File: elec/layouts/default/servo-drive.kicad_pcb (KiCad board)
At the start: 4 copper layers, 37.5 x 39.9 mm, 125 parts, among them U2 8Mhz

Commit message: Placement 90% complete
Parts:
- removed R2, R5: 10kOhm, Resistor_SMD:R_0402_1005Metric
- removed U19: , lib:SC-70-6_L2.1-W1.3-P0.65-LS2.1-BR
- added C23: 10uF, Capacitor_SMD:C_0603_1608Metric, F.Cu at (177.0, 101.6)
- C11, C20, C21, C22, C40, C5, R13, R14, R44, R45, R46, R50, R51, U21, U25, U26: moved to B.Cu
- C16: moved to F.Cu
- C26: footprint Capacitor_SMD:C_0805_2012Metric -> Capacitor_SMD:C_0603_1608Metric; moved to F.Cu
- C29: footprint Capacitor_SMD:C_0805_2012Metric -> Capacitor_SMD:C_0603_1608Metric
- C31, C32: value 22uF -> 10uF; footprint Capacitor_SMD:C_0805_2012Metric -> Capacitor_SMD:C_0603_1608Metric; moved to F.Cu
- C8: value (none) -> 10uF; footprint Capacitor_SMD:C_0402_1005Metric -> Capacitor_SMD:C_0603_1608Metric
- R12, R49: value (none) -> 45kOhm
- R25: value (none) -> 1kOhm; moved to B.Cu
- R26: value (none) -> 45kOhm; moved to B.Cu
- R48, R6: value (none) -> 1kOhm
- U17: footprint lib:CONN-SMD_4P-P1.00_SM04B-SRSS-TB-LF-SN -> lib:LED-SMD_4P-L4.0-W1.4_SK6805SIDE-S; moved to B.Cu
- U4: footprint lib:SOIC-8_L5.0-W4.0-P1.27-LS6.0-BL -> Package_TO_SOT_SMD:SOT-23-5
- moved C39 99.8 mm to (233.5, 85.1)
- moved R14 97.8 mm to (226.7, 86.9)
- moved C21 96.5 mm to (233.5, 85.4)
- moved R13 96.2 mm to (226.7, 87.9), turned to 180 degrees
- moved C20 96.0 mm to (233.5, 83.0)
- moved C22 90.7 mm to (233.8, 105.1)
- moved R45 82.8 mm to (226.7, 92.4)
- moved R44 82.1 mm to (226.7, 91.4), turned to 180 degrees
- moved C2 80.2 mm to (217.1, 111.3), turned to -90 degrees
- moved R1 80.1 mm to (217.1, 109.4), turned to -90 degrees
- moved R51 71.0 mm to (226.7, 105.0)
- moved R50 70.4 mm to (226.7, 104.0), turned to 180 degrees
- moved U25 68.2 mm to (213.0, 106.4)
- moved U27 56.9 mm to (210.9, 119.1)
- moved U4 56.6 mm to (219.3, 109.8), turned to 90 degrees
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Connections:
- C10 pad 1: servo_drive.ato:ServoDrive.power_stage.current_sense_a.out -> servo_drive.ato:ServoDrive.power_stage.i_fb_a
- C11 pad 1: servo_drive.ato:ServoDrive.power_stage.current_sense_b.out -> servo_drive.ato:ServoDrive.power_stage.i_fb_b
- C12 pad 1: servo_drive.ato:ServoDrive.power_stage.current_sense_c.out -> servo_drive.ato:ServoDrive.power_stage.i_fb_c
- C2 pad 1: servo_drive.ato:ServoDrive.power_stage.reference.buffer.in_p_a-filter.out -> servo_drive.ato:ServoDrive.power_stage.reference.buffer.in_p-filter.out
- C8 pad 1: servo_drive.ato:ServoDrive.power_stage.reference.buffer.in_p_b-half_ref.output -> servo_drive.ato:ServoDrive.v_10
- R1 pad 2: servo_drive.ato:ServoDrive.power_stage.reference.buffer.in_p_a-filter.out -> servo_drive.ato:ServoDrive.power_stage.reference.buffer.in_p-filter.out
- R14 pad 2: servo_drive.ato:ServoDrive.v_3 -> servo_drive.ato:ServoDrive.power_stage.v_ref
- R16 pad 2: servo_drive.ato:ServoDrive.power_stage.current_sense_a.out -> servo_drive.ato:ServoDrive.power_stage.i_fb_a
- R45 pad 2: servo_drive.ato:ServoDrive.v_3 -> servo_drive.ato:ServoDrive.power_stage.v_ref
- R46 pad 2: servo_drive.ato:ServoDrive.power_stage.current_sense_b.out -> servo_drive.ato:ServoDrive.power_stage.i_fb_b
- R51 pad 2: servo_drive.ato:ServoDrive.v_3 -> servo_drive.ato:ServoDrive.power_stage.v_ref
- R52 pad 2: servo_drive.ato:ServoDrive.power_stage.current_sense_c.out -> servo_drive.ato:ServoDrive.power_stage.i_fb_c
- U15 pad 38: servo_drive.ato:ServoDrive.micro_kit.micro.PA15 -> servo_drive.ato:ServoDrive.position_sensor.cs
- U15 pad 39: servo_drive.ato:ServoDrive.micro_kit.micro.PB3 -> servo_drive.ato:ServoDrive.position_sensor.sck
- U15 pad 40: servo_drive.ato:ServoDrive.micro_kit.micro.PB4 -> servo_drive.ato:ServoDrive.position_sensor.miso
- U15 pad 41: servo_drive.ato:ServoDrive.micro_kit.micro.PB5 -> servo_drive.ato:ServoDrive.position_sensor.mosi
- U15 pad 42: servo_drive.ato:ServoDrive.i2c_active_terminator.bus2-stemma.scl -> servo_drive.ato:ServoDrive.micro_kit.micro.PB6
- U15 pad 43: servo_drive.ato:ServoDrive.i2c_active_terminator.bus1-stemma.sda -> servo_drive.ato:ServoDrive.micro_kit.micro.PB7
- U17 pad 1: servo_drive.ato:ServoDrive.gnd -> servo_drive.ato:ServoDrive.v_5
- U17 pad 2: servo_drive.ato:ServoDrive.v_3 -> servo_drive.ato:ServoDrive.gnd
- U17 pad 3: servo_drive.ato:ServoDrive.i2c_active_terminator.bus1-stemma.sda -> servo_drive.ato:ServoDrive.led2.data_out
- U17 pad 4: servo_drive.ato:ServoDrive.i2c_active_terminator.bus2-stemma.scl -> servo_drive.ato:ServoDrive.led.data_out-led2.data_in
- U4 pad 1: servo_drive.ato:ServoDrive.power_stage.reference.buffer.in_n_a-out_a -> servo_drive.ato:ServoDrive.power_stage.reference.buffer.in_p-filter.out
- U4 pad 2: servo_drive.ato:ServoDrive.power_stage.reference.buffer.in_n_a-out_a -> servo_drive.ato:ServoDrive.gnd
- U4 pad 3: servo_drive.ato:ServoDrive.power_stage.reference.buffer.in_p_a-filter.out -> servo_drive.ato:ServoDrive.power_stage.v_ref
- U4 pad 4: servo_drive.ato:ServoDrive.gnd -> servo_drive.ato:ServoDrive.power_stage.v_ref
- U4 pad 5: servo_drive.ato:ServoDrive.power_stage.reference.buffer.in_p_b-half_ref.output -> servo_drive.ato:ServoDrive.v_3
- U5 pad 3: servo_drive.ato:ServoDrive.led.data_out -> servo_drive.ato:ServoDrive.led.data_out-led2.data_in
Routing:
- net servo_drive.ato:ServoDrive.canbus.CANL-canbus_conn_1.scl-canbus_conn_2.scl: track 0.00 -> 21.0 mm, vias 0 -> 1
- net servo_drive.ato:ServoDrive.canbus.CANH-canbus_conn_1.sda-canbus_conn_2.sda: track 0.00 -> 11.0 mm, vias 0 -> 1
- net servo_drive.ato:ServoDrive.v_3: track 1.30 -> 7.06 mm
- net servo_drive.ato:ServoDrive.buck.SGND: track 5.24 -> 10.6 mm, vias 0 -> 2
- net servo_drive.ato:ServoDrive.buck.buck_converter.VCC: track 0.00 -> 5.29 mm
- net servo_drive.ato:ServoDrive.micro_kit.osc.out: track 0.00 -> 4.74 mm
- net servo_drive.ato:ServoDrive.micro_kit.micro.PD0_OSC_IN-osc.in: track 0.00 -> 4.74 mm
- net servo_drive.ato:ServoDrive.micro_kit.micro.PD1_OSC_OUT: track 0.00 -> 4.26 mm
- net servo_drive.ato:ServoDrive.power_stage.current_sense_c.feedback_div.gnd-opamp.out-output_filter.in: track 0.00 -> 4.03 mm
- net servo_drive.ato:ServoDrive.power_stage.current_sense_c.feedback_div.output-opamp.in_n: track 0.00 -> 3.55 mm
- net servo_drive.ato:ServoDrive.gnd: track 30.9 -> 27.7 mm, vias 38 -> 37
- net servo_drive.ato:ServoDrive.power_stage.current_sense_c.bias_div.output-opamp.in_p: track 0.00 -> 2.45 mm
- net servo_drive.ato:ServoDrive.power_stage.v_ref: track 0.00 -> 2.28 mm
- net servo_drive.ato:ServoDrive.power_stage.reference.buffer.in_p-filter.out: track 0.00 -> 2.20 mm
- net servo_drive.ato:ServoDrive.buck.buck_converter.SS: track 0.00 -> 1.95 mm
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
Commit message: layout
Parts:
- removed C33: , Capacitor_SMD:C_0402_1005Metric
- removed C34: 2nF, Capacitor_SMD:C_0402_1005Metric
- removed R27: 10kOhm, Resistor_SMD:R_0402_1005Metric
- removed R28: 1kOhm, Resistor_SMD:R_0402_1005Metric
- C1, C18, C3, C8, R24: moved to B.Cu
- moved C8 64.6 mm to (240.2, 112.3), turned to -90 degrees
- moved C19 54.7 mm to (213.1, 100.8), turned to 180 degrees
- moved C1 48.6 mm to (213.1, 101.8), turned to 180 degrees
- moved C18 46.4 mm to (207.4, 94.9), turned to -90 degrees
- moved C23 42.7 mm to (219.6, 97.3), turned to -90 degrees
- moved C32 41.1 mm to (221.0, 90.7), turned to -90 degrees
- moved S1 39.1 mm to (213.8, 88.7)
- moved C3 38.2 mm to (216.9, 96.3), turned to -45 degrees
- moved R24 37.8 mm to (218.9, 84.2), turned to 45 degrees
- moved R11 33.1 mm to (207.9, 88.5), turned to -90 degrees
- moved C31 29.6 mm to (220.9, 101.6), turned to 90 degrees
- moved C5 28.7 mm to (241.6, 111.8), turned to -90 degrees
- moved C17 26.4 mm to (214.4, 114.3)
- moved C13 25.7 mm to (214.3, 113.3)
- moved R23 25.2 mm to (208.0, 92.4), turned to 90 degrees
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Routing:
- net servo_drive.ato:ServoDrive.micro_kit.micro.PD0_OSC_IN-osc.in: track 4.74 -> 6.66 mm
- net servo_drive.ato:ServoDrive.gnd: track 27.7 -> 29.3 mm

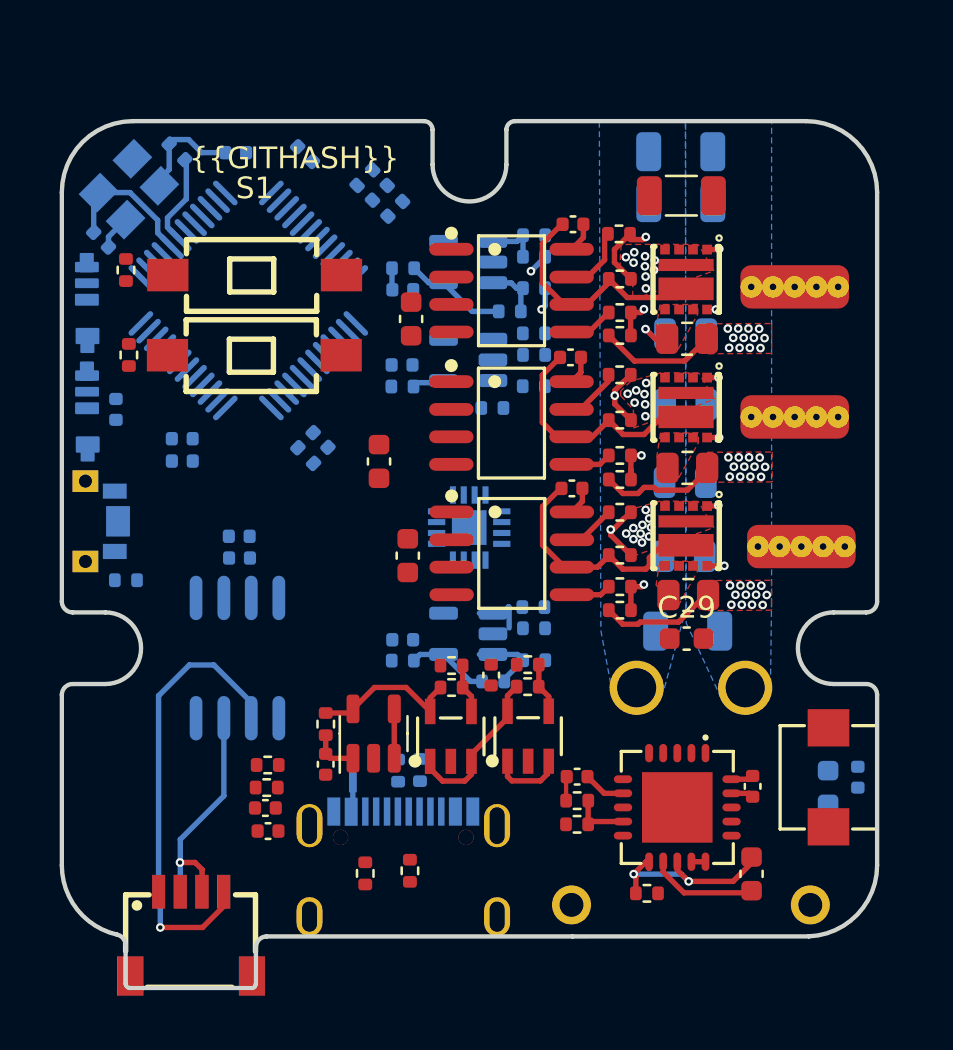
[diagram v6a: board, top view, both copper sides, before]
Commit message: swapped out big boi caps for 0805s, finished most of the routing
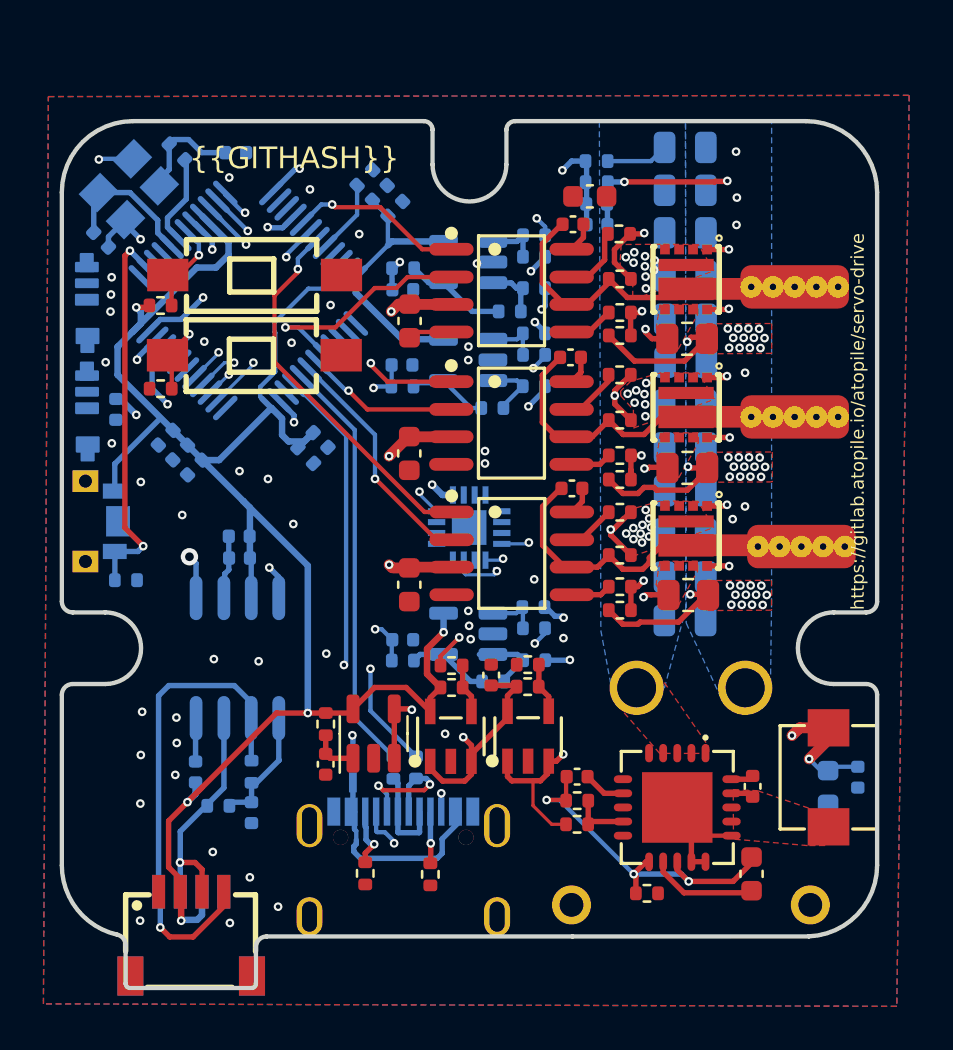
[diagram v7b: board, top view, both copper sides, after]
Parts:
- added C24: 10uF, Capacitor_SMD:C_0805_2012Metric, B.Cu at (233.7, 88.8)
- added C25: 10uF, Capacitor_SMD:C_0805_2012Metric, B.Cu at (233.7, 96.7)
- added C27: 10uF, Capacitor_SMD:C_0805_2012Metric, B.Cu at (233.7, 98.7)
- added C33: , Capacitor_SMD:C_0402_1005Metric, B.Cu at (229.6, 86.4)
- added C34: 2nF, Capacitor_SMD:C_0402_1005Metric, B.Cu at (229.6, 85.4)
- added C36: 10uF, Capacitor_SMD:C_0805_2012Metric, B.Cu at (233.6, 104.6)
- added R27: 10kOhm, Resistor_SMD:R_0402_1005Metric, B.Cu at (229.6, 83.5)
- added R28: 1kOhm, Resistor_SMD:R_0402_1005Metric, B.Cu at (229.6, 84.4)
- added U17: , lib:NetTie-2_SMD_Pad0.25mm, F.Cu at (232.1, 91.7)
- added U19: , lib:NetTie-2_SMD_Pad0.25mm, F.Cu at (233.9, 91.6)
- added U30: , lib:NetTie-2_SMD_Pad0.25mm, F.Cu at (232.0, 97.6)
- added U31: , lib:NetTie-2_SMD_Pad0.25mm, F.Cu at (233.9, 97.6)
- added U32: , lib:NetTie-2_SMD_Pad0.25mm, F.Cu at (232.1, 103.4)
- added U33: , lib:NetTie-2_SMD_Pad0.25mm, F.Cu at (233.9, 103.4)
- C13, C17, R53, R54: moved to B.Cu
- C20, C21, C22: footprint Capacitor_SMD:C_1206_3216Metric -> Capacitor_SMD:C_0805_2012Metric
- C39: footprint Capacitor_SMD:C_1206_3216Metric -> Capacitor_SMD:C_0805_2012Metric; moved to B.Cu
- moved C29 20.8 mm to (229.3, 85.1), turned to 180 degrees
- moved C9 15.3 mm to (211.1, 97.6), turned to -135 degrees
- moved C13 3.62 mm to (211.1, 111.6), turned to 90 degrees
- moved C44 3.55 mm to (233.7, 94.7)
- moved R53 2.95 mm to (212.2, 113.2)
- moved C22 2.49 mm to (233.7, 102.6)
- moved R11 2.28 mm to (209.5, 90.1), turned to 0 degrees
- moved R23 2.13 mm to (209.5, 94.0), turned to 180 degrees
- moved C28 1.95 mm to (233.7, 92.7)
- moved C39 1.72 mm to (233.7, 86.8)
- moved C23 1.44 mm to (220.9, 96.9)
- moved C31 1.34 mm to (221.0, 103.0), turned to -90 degrees
- moved C17 1.14 mm to (213.7, 113.5), turned to -90 degrees
- moved C42 1.04 mm to (233.6, 100.6)
- moved R54 1.01 mm to (213.7, 111.6), turned to -90 degrees
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- renumbered U17 to U29
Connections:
- R13 pad 1: servo_drive.ato:ServoDrive.power_stage.current_sense_a.i_in-half_bridge_a.pwr_gnd -> servo_drive.ato:ServoDrive.power_stage.current_sense_a.bias_div.input-nt_p.p1
- R25 pad 1: servo_drive.ato:ServoDrive.gnd -> servo_drive.ato:ServoDrive.power_stage.current_sense_b.feedback_div.input-nt_n.p1
- R44 pad 1: servo_drive.ato:ServoDrive.power_stage.current_sense_b.i_in-half_bridge_b.pwr_gnd -> servo_drive.ato:ServoDrive.power_stage.current_sense_b.bias_div.input-nt_p.p1
- R48 pad 1: servo_drive.ato:ServoDrive.gnd -> servo_drive.ato:ServoDrive.power_stage.current_sense_c.feedback_div.input-nt_n.p1
- R50 pad 1: servo_drive.ato:ServoDrive.power_stage.current_sense_c.i_in-half_bridge_c.pwr_gnd -> servo_drive.ato:ServoDrive.power_stage.current_sense_c.bias_div.input-nt_p.p1
- R6 pad 1: servo_drive.ato:ServoDrive.gnd -> servo_drive.ato:ServoDrive.power_stage.current_sense_a.feedback_div.input-nt_n.p1
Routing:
- net servo_drive.ato:ServoDrive.v_3: track 7.06 -> 110.1 mm, vias 0 -> 6
- net servo_drive.ato:ServoDrive.v_10: track 3.72 -> 62.3 mm, vias 0 -> 6
- net servo_drive.ato:ServoDrive.power_stage.v_ref: track 2.28 -> 34.6 mm, vias 0 -> 4
- net servo_drive.ato:ServoDrive.v_5: track 7.50 -> 39.2 mm, vias 0 -> 3
- net servo_drive.ato:ServoDrive.power_stage.i_fb_c: track 0.00 -> 25.7 mm, vias 0 -> 2
- net servo_drive.ato:ServoDrive.position_sensor.miso: track 0.00 -> 21.6 mm, vias 0 -> 2
- net servo_drive.ato:ServoDrive.position_sensor.mosi: track 0.00 -> 20.8 mm, vias 0 -> 2
- net servo_drive.ato:ServoDrive.voltage_input_vdiv.out: track 0.00 -> 20.2 mm, vias 0 -> 2
- net servo_drive.ato:ServoDrive.micro_kit.micro.PA12: track 0.00 -> 20.2 mm, vias 0 -> 2
- net servo_drive.ato:ServoDrive.gnd: track 29.3 -> 49.0 mm, vias 37 -> 90
- net servo_drive.ato:ServoDrive.position_sensor.cs: track 0.00 -> 19.4 mm, vias 0 -> 2
- net servo_drive.ato:ServoDrive.micro_kit.micro.PA11: track 0.00 -> 19.2 mm
- net servo_drive.ato:ServoDrive.switch.pin1: track 0.00 -> 18.0 mm, vias 0 -> 2
- net servo_drive.ato:ServoDrive.power_stage.low_in_c: track 0.00 -> 17.5 mm, vias 0 -> 1
- net servo_drive.ato:ServoDrive.led.data_in: track 0.00 -> 14.3 mm, vias 0 -> 2
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- added copper zone on F.Cu, net servo_drive.ato:ServoDrive.buck.buck_converter.LX
- added copper zone on In1.Cu, net servo_drive.ato:ServoDrive.gnd
